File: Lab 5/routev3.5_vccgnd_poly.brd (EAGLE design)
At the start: 100 x 80 mm, 48 parts, among them J1 FTDI_DEVICERA_SMT, M1 WIRELESS-NRF24L01, U1 3.3V, U2 GY-521MPU6050

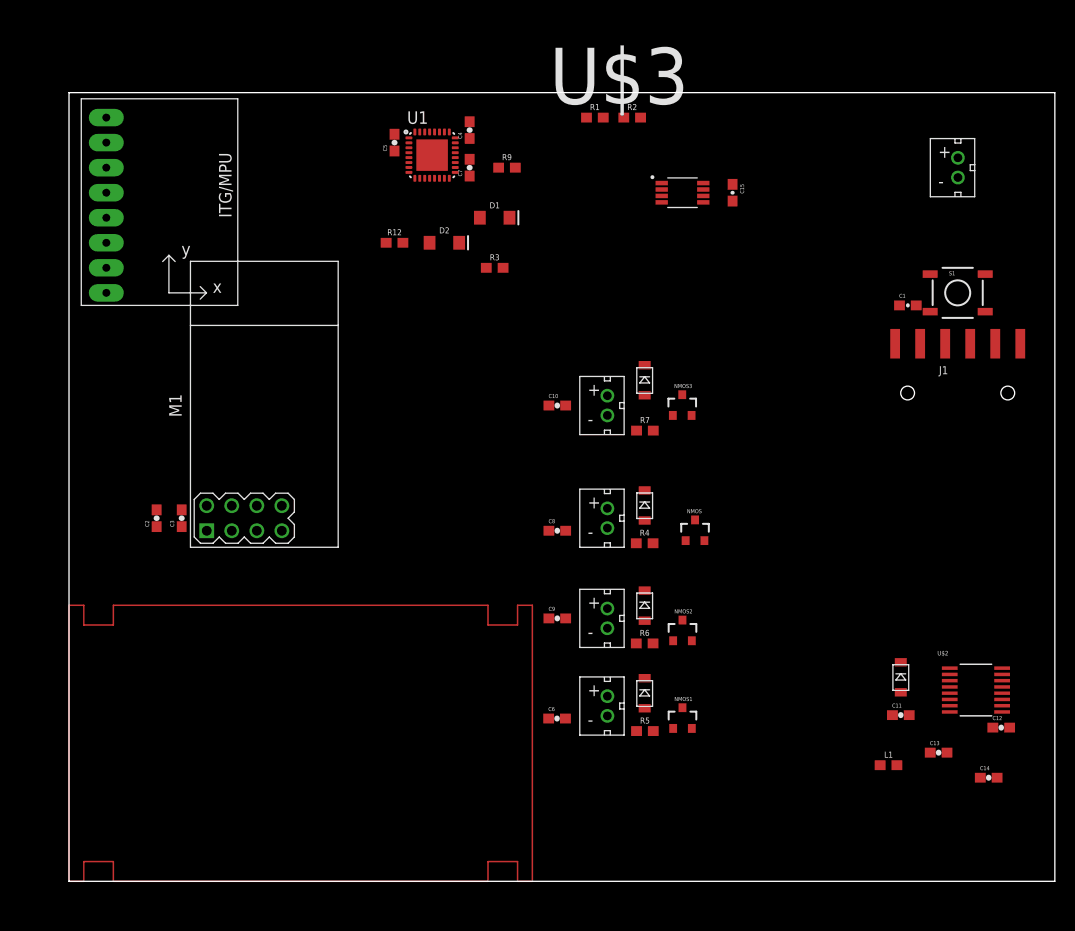
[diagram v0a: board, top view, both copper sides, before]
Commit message: Update template file, switch for the right Atmega MCU. Some advice from Arti:   - Everything need to be inside the board (all white frames inside): quadcopter propellers need clearance.   - Nothing under white frame except the Radio Module   - Battery JBT need to have +- on the edge of the PCB   - Mandatory: Top Polygon: VCC, Bottom Polygon: GND; Don't worry about Digital and Analog VCC and GND.
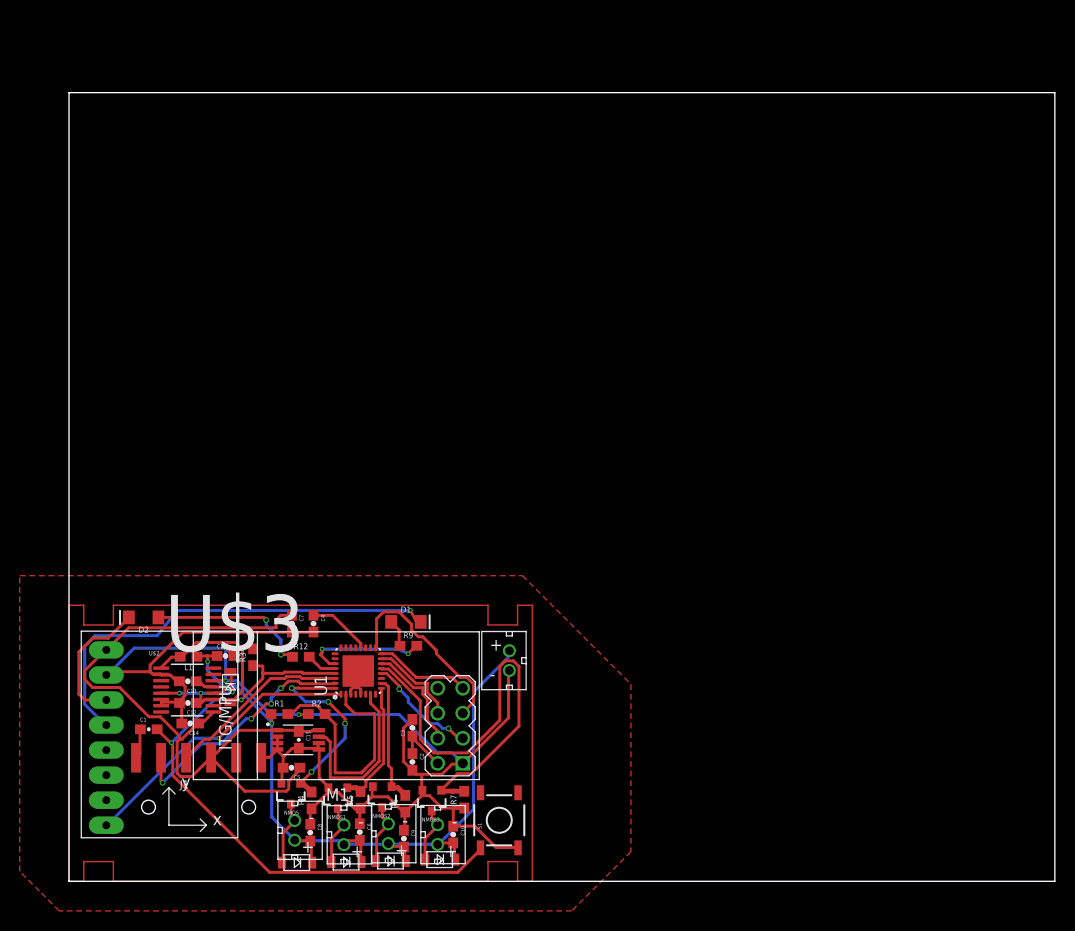
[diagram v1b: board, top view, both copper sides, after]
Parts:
- moved C1 88.2 mm to (8.09, 15.4)
- moved J1 87.7 mm to (13.1, 7.53)
- moved C12 82.5 mm to (12.1, 18.1), turned to 180 degrees
- moved C14 81.2 mm to (12.3, 16.0), turned to 180 degrees
- moved U$2 80.0 mm to (12.0, 19.4)
- moved C13 76.5 mm to (12.1, 20.3), turned to 180 degrees
- moved L1 71.8 mm to (12.1, 22.8), turned to 180 degrees
- moved S1 70.9 mm to (43.6, 6.19), turned to 90 degrees
- moved C15 70.8 mm to (23.3, 14.3)
- moved C11 68.8 mm to (15.9, 22.9)
- moved R1 68.4 mm to (21.3, 17.0)
- moved R2 68.4 mm to (25.1, 17.0)
- moved DIODE4 68.0 mm to (16.4, 19.7)
- moved U$3 67.8 mm to (23.2, 14.3)
- moved U$1 67.6 mm to (44.7, 22.4)
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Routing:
- net GND: track 0.00 -> 163.3 mm, vias 0 -> 3
- net BATTERY+: track 0.00 -> 80.0 mm, vias 0 -> 3
- net VCC: track 0.00 -> 79.4 mm
- net RESET: track 0.00 -> 63.5 mm, vias 0 -> 2
- net MOTOR4: track 0.00 -> 46.1 mm
- net IMU-SDA: track 0.00 -> 45.5 mm, vias 0 -> 1
- net IMU-INT: track 0.00 -> 29.3 mm, vias 0 -> 1
- net FTDI-TX: track 0.00 -> 25.0 mm, vias 0 -> 4
- net MEASURE_PIN: track 0.00 -> 24.5 mm
- net MOTOR1: track 0.00 -> 21.0 mm, vias 0 -> 4
- net RF-SCK: track 0.00 -> 20.1 mm
- net FTDI-RX: track 0.00 -> 18.6 mm
- net OSC1: track 0.00 -> 17.9 mm
- net N$9: track 0.00 -> 16.4 mm, vias 0 -> 2
- net N$1: track 0.00 -> 15.6 mm
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- added copper zone on layer 1, net N$12
